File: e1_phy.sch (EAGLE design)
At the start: 127 parts, among them IC2 LD117AS33TR, IC3 LD117AS33TR, U1 IDT82V2081, U2 GPS_GNS_2201, U3 VCTCXO-CONNORWINFIELD, U4 VCXO_TAITIEN_VT, U5 IP4234CZ6, U7 IP4234CZ6, X2 SMA-142-0701-801/806, X3 JACK2.5_SJ-2523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

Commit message: Moved LIU VDD_analog from +UB to Vcc+Inductor
(this is suggested in the datasheet, and I don't want to
 pollute the +UB (clean supply for oscillators))
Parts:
- added L2: 10uH, rcl:L-EUL1812
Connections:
- new net LIU_VDDA: C29.1, L2.2, U1.VDDA
- net +UB: no longer C29.1, U1.VDDA
- net VCC: now also L2.1
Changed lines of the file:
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@@
 <part name="P+1" library="supply1" deviceset="VCC" device=""/>
 <part name="P+2" library="supply1" deviceset="VCC" device=""/>
-<part name="SUPPLY9" library="supply2" deviceset="+UB" device=""/>
 <part name="GND5" library="supply1" deviceset="GND" device=""/>
 <part name="P+3" library="supply1" deviceset="VCC" device=""/>
@@
 <part name="P+5" library="supply1" deviceset="VCC" device=""/>
 <part name="GND4" library="supply1" deviceset="GND" device=""/>
-<part name="SUPPLY10" library="supply2" deviceset="+UB" device=""/>
 <part name="C29" library="rcl" deviceset="C-EU" device="C0603" value="100n"/>
 <part name="P+6" library="supply1" deviceset="VCC" device=""/>
@@
 <part name="R11" library="rcl" deviceset="R-EU_" device="R0603" value="10k"/>
 <part name="P+20" library="supply1" deviceset="VCC" device=""/>
+<part name="L2" library="rcl" deviceset="L-EU" device="L1812" value="10uH"/>
+<part name="P+21" library="supply1" deviceset="VCC" device=""/>
 </parts>
 <sheets>
@@
 <instance part="P+1" gate="VCC" x="256.54" y="73.66"/>
 <instance part="P+2" gate="VCC" x="195.58" y="73.66"/>
-<instance part="SUPPLY9" gate="G$1" x="187.96" y="73.66"/>
 <instance part="GND5" gate="1" x="233.68" y="83.82" smashed="yes" rot="R180">
 <attribute name="VALUE" x="233.68" y="86.36" size="1.778" layer="96" rot="R90"/>
@@
 <attribute name="VALUE" x="254" y="96.52" size="1.778" layer="96"/>
 </instance>
-<instance part="SUPPLY10" gate="G$1" x="271.78" y="121.92"/>
 <instance part="C29" gate="G$1" x="271.78" y="111.76" rot="MR0"/>
 <instance part="P+6" gate="VCC" x="327.66" y="111.76" rot="R270"/>
@@
 <instance part="R11" gate="G$1" x="170.18" y="63.5" rot="R90"/>
 <instance part="P+20" gate="VCC" x="170.18" y="73.66"/>
+<instance part="L2" gate="G$1" x="185.42" y="73.66"/>
+<instance part="P+21" gate="VCC" x="185.42" y="83.82"/>
 </instances>
 <busses>
@@
 <pinref part="P+20" gate="VCC" pin="VCC"/>
 </segment>
+<segment>
+<pinref part="P+21" gate="VCC" pin="VCC"/>
+<pinref part="L2" gate="G$1" pin="1"/>
+<wire x1="185.42" y1="81.28" x2="185.42" y2="78.74" width="0.1524" layer="91"/>
+</segment>
 </net>
 <net name="CLK2048" class="0">
@@
 <pinref part="SUPPLY8" gate="G$1" pin="+UB"/>
 <wire x1="363.22" y1="116.84" x2="363.22" y2="114.3" width="0.1524" layer="91"/>
-</segment>
-<segment>
-<pinref part="U1" gate="G$1" pin="VDDA"/>
-<wire x1="198.12" y1="66.04" x2="187.96" y2="66.04" width="0.1524" layer="91"/>
-<pinref part="SUPPLY9" gate="G$1" pin="+UB"/>
-<wire x1="187.96" y1="66.04" x2="187.96" y2="71.12" width="0.1524" layer="91"/>
-</segment>
-<segment>
-<pinref part="C29" gate="G$1" pin="1"/>
-<pinref part="SUPPLY10" gate="G$1" pin="+UB"/>
-<wire x1="271.78" y1="114.3" x2="271.78" y2="119.38" width="0.1524" layer="91"/>
 </segment>
 </net>
@@
 </segment>
 </net>
+<net name="LIU_VDDA" class="0">
+<segment>
+<pinref part="C29" gate="G$1" pin="1"/>
+<wire x1="271.78" y1="114.3" x2="271.78" y2="116.84" width="0.1524" layer="91"/>
+<wire x1="271.78" y1="116.84" x2="281.94" y2="116.84" width="0.1524" layer="91"/>
+<label x="272.034" y="117.348" size="1.27" layer="95"/>
+</segment>
+<segment>
+<pinref part="U1" gate="G$1" pin="VDDA"/>
+<wire x1="198.12" y1="66.04" x2="185.42" y2="66.04" width="0.1524" layer="91"/>
+<pinref part="L2" gate="G$1" pin="2"/>
+<wire x1="185.42" y1="68.58" x2="185.42" y2="66.04" width="0.1524" layer="91"/>
+<wire x1="177.8" y1="66.04" x2="185.42" y2="66.04" width="0.1524" layer="91"/>
+<junction x="185.42" y="66.04"/>
+<label x="175.768" y="66.294" size="1.27" layer="95"/>
+</segment>
+</net>

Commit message: Review comments: Add ESD protection on GPS antenna.
0603ESDA-TR from laforge library.
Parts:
- removed R32: 27k, rcl:R-EU_R0603
- removed R33: 47k, rcl:R-EU_R0603
- added D10: 0603ESDA-TR, laforge:0603ESDA-TR
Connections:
- removed net USB_VBUS_SENS: R32.1, R33.2
- net GND: now also D10.K; no longer R33.1
- net N$4: now also D10.A
- net VBUS_CONN: no longer R32.2
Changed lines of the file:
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@@
 <part name="R30" library="rcl" deviceset="R-EU_" device="R0603" value="33R"/>
 <part name="R31" library="rcl" deviceset="R-EU_" device="R0603" value="33R"/>
-<part name="R32" library="rcl" deviceset="R-EU_" device="R0603" value="27k"/>
-<part name="R33" library="rcl" deviceset="R-EU_" device="R0603" value="47k"/>
 <part name="GND14" library="supply1" deviceset="GND" device=""/>
-<part name="GND15" library="supply1" deviceset="GND" device=""/>
 <part name="R34" library="rcl" deviceset="R-EU_" device="R0603" value="DNP"/>
 <part name="U2" library="cvogel" deviceset="GPS_GNS_2201" device=""/>
@@
 <part name="L2" library="rcl" deviceset="L-EU" device="L1812" value="10uH"/>
 <part name="P+21" library="supply1" deviceset="VCC" device=""/>
+<part name="D10" library="laforge" deviceset="0603ESDA-TR" device=""/>
+<part name="GND15" library="supply1" deviceset="GND" device=""/>
 </parts>
 <sheets>
@@
 <instance part="R30" gate="G$1" x="68.58" y="241.3" rot="R180"/>
 <instance part="R31" gate="G$1" x="68.58" y="233.68" rot="R180"/>
-<instance part="R32" gate="G$1" x="66.04" y="248.92" rot="R180"/>
-<instance part="R33" gate="G$1" x="81.28" y="243.84" rot="R180"/>
 <instance part="GND14" gate="1" x="27.94" y="228.6"/>
-<instance part="GND15" gate="1" x="91.44" y="243.84" rot="R90"/>
 <instance part="R34" gate="G$1" x="129.54" y="208.28" rot="R270"/>
 <instance part="U2" gate="G$1" x="327.66" y="238.76"/>
@@
 <instance part="L2" gate="G$1" x="185.42" y="73.66"/>
 <instance part="P+21" gate="VCC" x="185.42" y="83.82"/>
+<instance part="D10" gate="G$1" x="297.18" y="256.54"/>
+<instance part="GND15" gate="1" x="304.8" y="261.62" rot="R90"/>
 </instances>
 <busses>
@@
 <wire x1="68.58" y1="149.86" x2="66.04" y2="149.86" width="0.1524" layer="91"/>
 <wire x1="66.04" y1="149.86" x2="66.04" y2="147.32" width="0.1524" layer="91"/>
-</segment>
-<segment>
-<pinref part="GND15" gate="1" pin="GND"/>
-<pinref part="R33" gate="G$1" pin="1"/>
-<wire x1="88.9" y1="243.84" x2="86.36" y2="243.84" width="0.1524" layer="91"/>
 </segment>
 <segment>
@@
 <wire x1="355.6" y1="55.88" x2="355.6" y2="53.34" width="0.1524" layer="91"/>
 </segment>
+<segment>
+<pinref part="D10" gate="G$1" pin="K"/>
+<wire x1="297.18" y1="259.08" x2="297.18" y2="261.62" width="0.1524" layer="91"/>
+<wire x1="297.18" y1="261.62" x2="302.26" y2="261.62" width="0.1524" layer="91"/>
+<pinref part="GND15" gate="1" pin="GND"/>
+</segment>
 </net>
 <net name="LINE_PIN1" class="0">
@@
 </segment>
 </net>
-<net name="USB_VBUS_SENS" class="0">
-<segment>
-<pinref part="R32" gate="G$1" pin="1"/>
-<wire x1="71.12" y1="248.92" x2="73.66" y2="248.92" width="0.1524" layer="91"/>
-<pinref part="R33" gate="G$1" pin="2"/>
-<wire x1="73.66" y1="248.92" x2="86.36" y2="248.92" width="0.1524" layer="91"/>
-<wire x1="76.2" y1="243.84" x2="73.66" y2="243.84" width="0.1524" layer="91"/>
-<wire x1="73.66" y1="243.84" x2="73.66" y2="248.92" width="0.1524" layer="91"/>
-<junction x="73.66" y="248.92"/>
-<label x="76.2" y="249.174" size="1.27" layer="95"/>
-</segment>
-</net>
 <net name="USB_DDP" class="0">
 <segment>
@@
 <pinref part="X2" gate="G1" pin="1"/>
 <pinref part="U2" gate="G$1" pin="RF_IN"/>
-<wire x1="287.02" y1="251.46" x2="309.88" y2="251.46" width="0.1524" layer="91"/>
+<wire x1="287.02" y1="251.46" x2="297.18" y2="251.46" width="0.1524" layer="91"/>
+<pinref part="D10" gate="G$1" pin="A"/>
+<wire x1="297.18" y1="251.46" x2="309.88" y2="251.46" width="0.1524" layer="91"/>
+<wire x1="297.18" y1="254" x2="297.18" y2="251.46" width="0.1524" layer="91"/>
+<junction x="297.18" y="251.46"/>
 </segment>
 </net>
@@
 <net name="VBUS_CONN" class="0">
 <segment>
-<pinref part="R32" gate="G$1" pin="2"/>
-<wire x1="60.96" y1="248.92" x2="58.42" y2="248.92" width="0.1524" layer="91"/>
 <wire x1="25.4" y1="248.92" x2="25.4" y2="256.54" width="0.1524" layer="91"/>
 <pinref part="CN1" gate="G$1" pin="VBUS"/>
 <wire x1="22.86" y1="248.92" x2="25.4" y2="248.92" width="0.1524" layer="91"/>
 <pinref part="D1" gate="G$1" pin="A"/>
-<wire x1="63.5" y1="256.54" x2="58.42" y2="256.54" width="0.1524" layer="91"/>
-<wire x1="58.42" y1="256.54" x2="43.18" y2="256.54" width="0.1524" layer="91"/>
+<wire x1="63.5" y1="256.54" x2="43.18" y2="256.54" width="0.1524" layer="91"/>
 <wire x1="43.18" y1="256.54" x2="25.4" y2="256.54" width="0.1524" layer="91"/>
-<wire x1="58.42" y1="248.92" x2="58.42" y2="256.54" width="0.1524" layer="91"/>
-<junction x="58.42" y="256.54"/>
 <pinref part="U5" gate="G$1" pin="VCC"/>
 <wire x1="43.18" y1="254" x2="43.18" y2="256.54" width="0.1524" layer="91"/>

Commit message: Regenerated v7 eagle files, made .pdf for schematic.
 -> next release candidate 20180703
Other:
- note added: "e1_sam4_usb vogelchr@vogel.cx 2018-07-03 for review"
- note removed: "e1_sam4_usb vogelchr@vogel.cx 2018-06-25 for review"

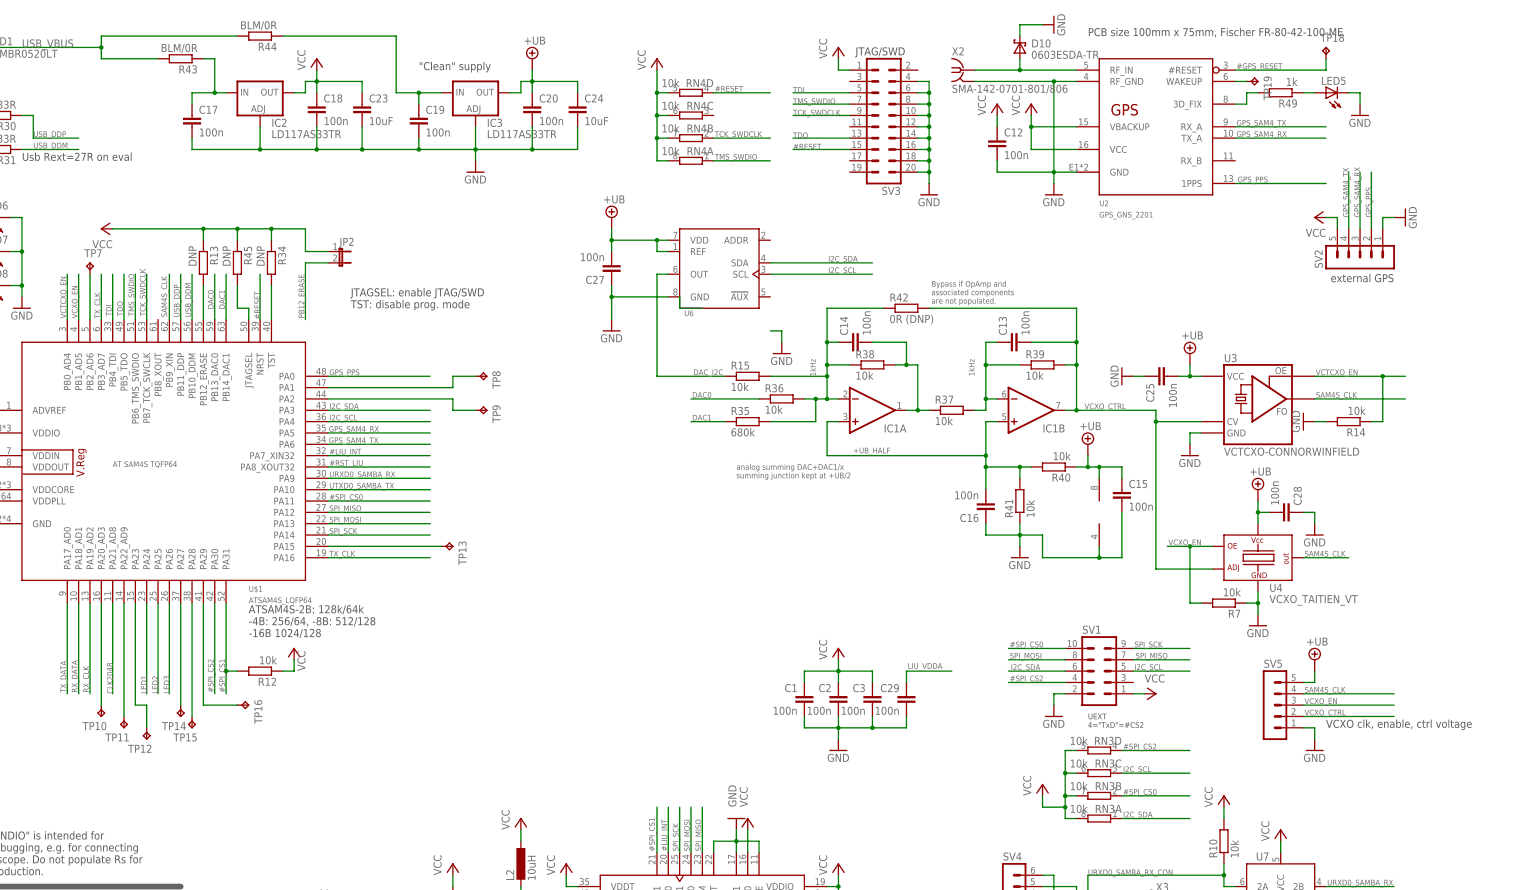
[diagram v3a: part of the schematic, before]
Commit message: 33R series resistor in clocks, RX/TX of PPS, SMA through hole
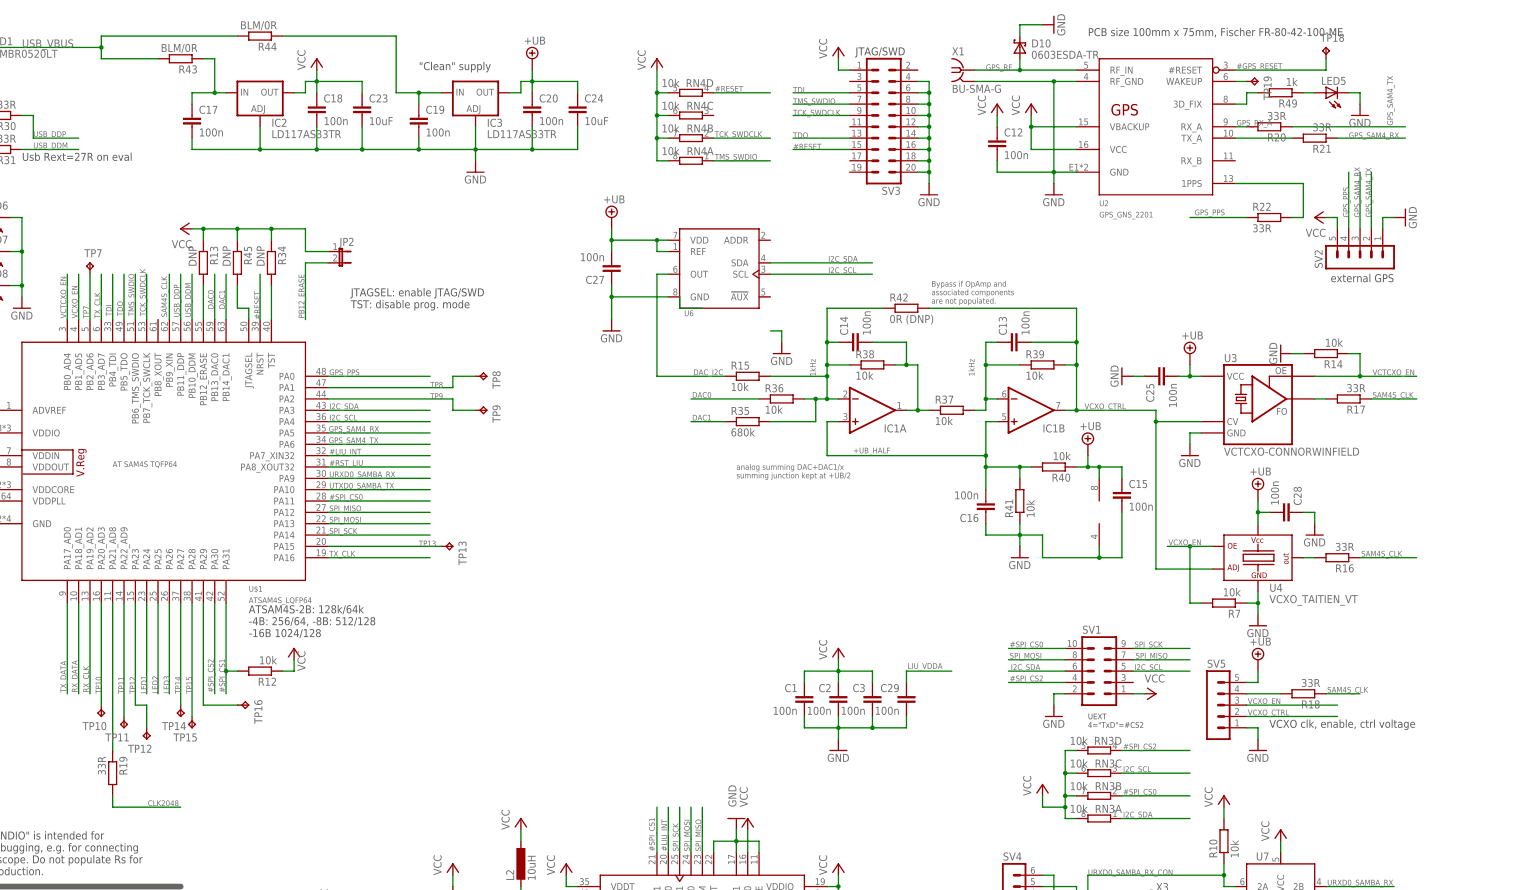
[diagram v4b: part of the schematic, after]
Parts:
- removed X2: SMA-142-0701-801/806, con-coax:SMA-142-0701-801/806
- added R16, R17, R18, R19, R20, R21, R22: 33R, rcl:R-EU_R0603
- added X1: BU-SMA-G, con-coax:BU-SMA-G
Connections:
- net N$10 renamed GPS_3DFIX
- net N$19 renamed TP12
- net N$20 renamed TP13
- net N$21 renamed TP7
- net N$22 renamed TP14
- net N$23 renamed TP15
- net N$24 renamed GPS_WAKEUP
- net N$6 renamed TP9
- net N$7 renamed TP8
- net N$8 renamed TP10
- net N$9 renamed TP11
- removed net N$4: D10.A, U2.RF_IN, X2.1
- new net CLK2048_SAM4S: R19.1, U$1.PA21_AD8
- new net GPS_RF: D10.A, U2.RF_IN, X1.1
- new net GPS_RX_A: R20.2, U2.RX_A
- new net N$30: R22.2, U2.1PPS
- new net SAM4S_CLK_EXT: R18.2, SV5.4
- new net SAM4S_CLK_VCTXO: R17.2, U3.FO
- new net SAM4S_CLK_VCXO: R16.2, U4.Q
- new net TPS_TX_A: R21.2, U2.TX_A
- net CLK2048: now also R19.2; no longer U$1.PA21_AD8
- net GND: now also X1.2; no longer X2.2
- net GPS_PPS: now also R22.1, SV2.4; no longer SV2.2, U2.1PPS
- net GPS_SAM4_RX: now also R21.1; no longer U2.TX_A
- net GPS_SAM4_TX: now also R20.1, SV2.2; no longer SV2.4, U2.RX_A
- net SAM4S_CLK: now also R16.1, R17.1, R18.1; no longer SV5.4, U3.FO, U4.Q
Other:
- moved on the sheet: R14, SV5
